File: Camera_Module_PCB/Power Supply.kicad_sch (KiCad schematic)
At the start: 27 parts, among them J1 SS-52400-002, SW1 SW_DIP_x01

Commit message: no
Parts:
- R5, R6, R7: value R_US -> 1K
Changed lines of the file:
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@@
 			)
 		)
-		(property "Value" "R_US"
+		(property "Value" "1K"
 			(at 139.7 71.1199 0)
 			(effects
@@
 			)
 		)
-		(property "Value" "R_US"
+		(property "Value" "1K"
 			(at 148.59 71.1199 0)
 			(effects
@@
 			)
 		)
-		(property "Value" "R_US"
+		(property "Value" "1K"
 			(at 157.48 71.1199 0)
 			(effects

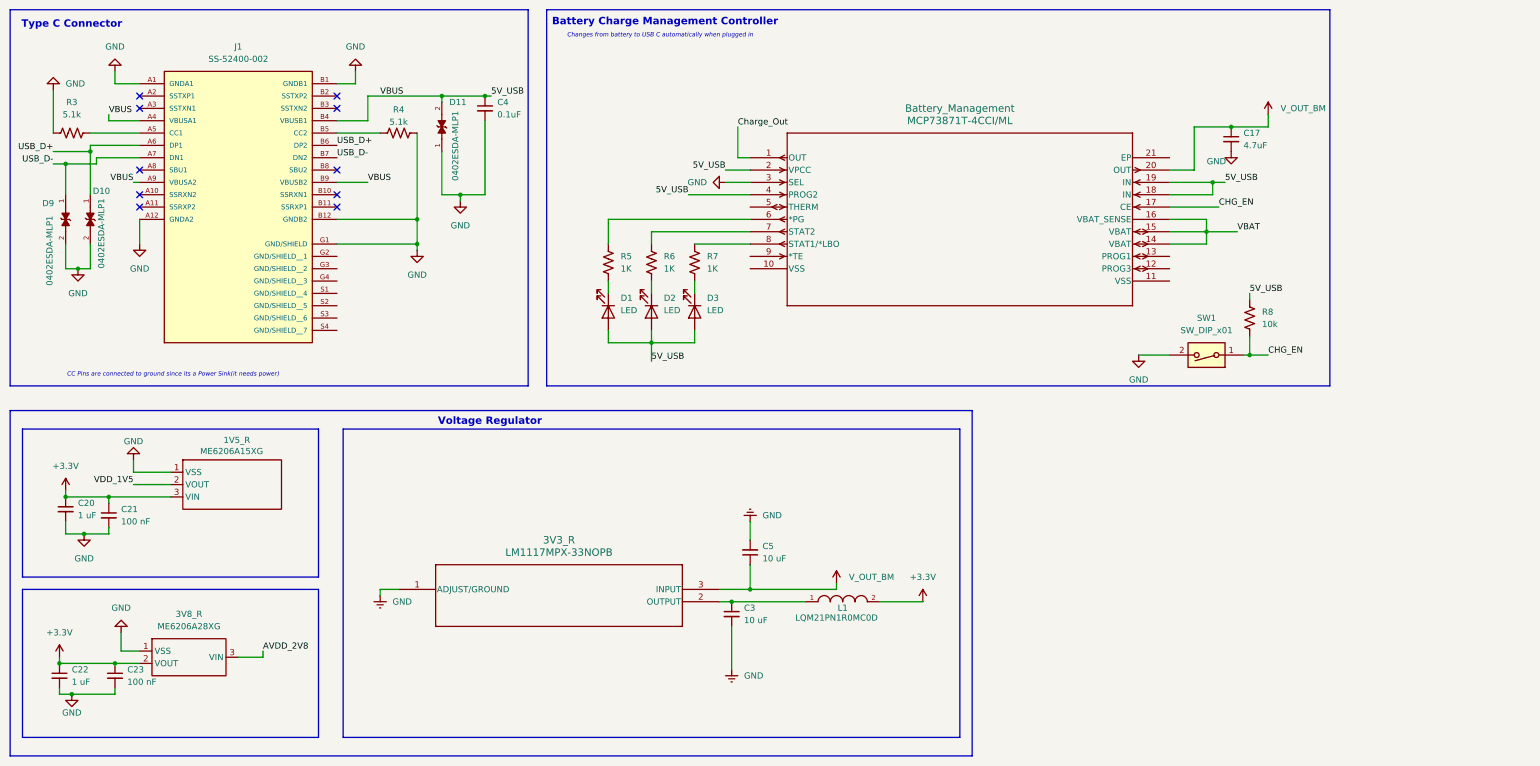
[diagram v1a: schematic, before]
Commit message: Compiled Footprints and Set up PCB layout
All of the footprints that correspond to the schematic symbols were properly referenced in the schematic annotations. The PCB layout was then updated to contain all of the appropriate footprints. Finally, a large ground filled zone was created with dimensions of about 42mm x 42mm as a starting base for the PCB size.
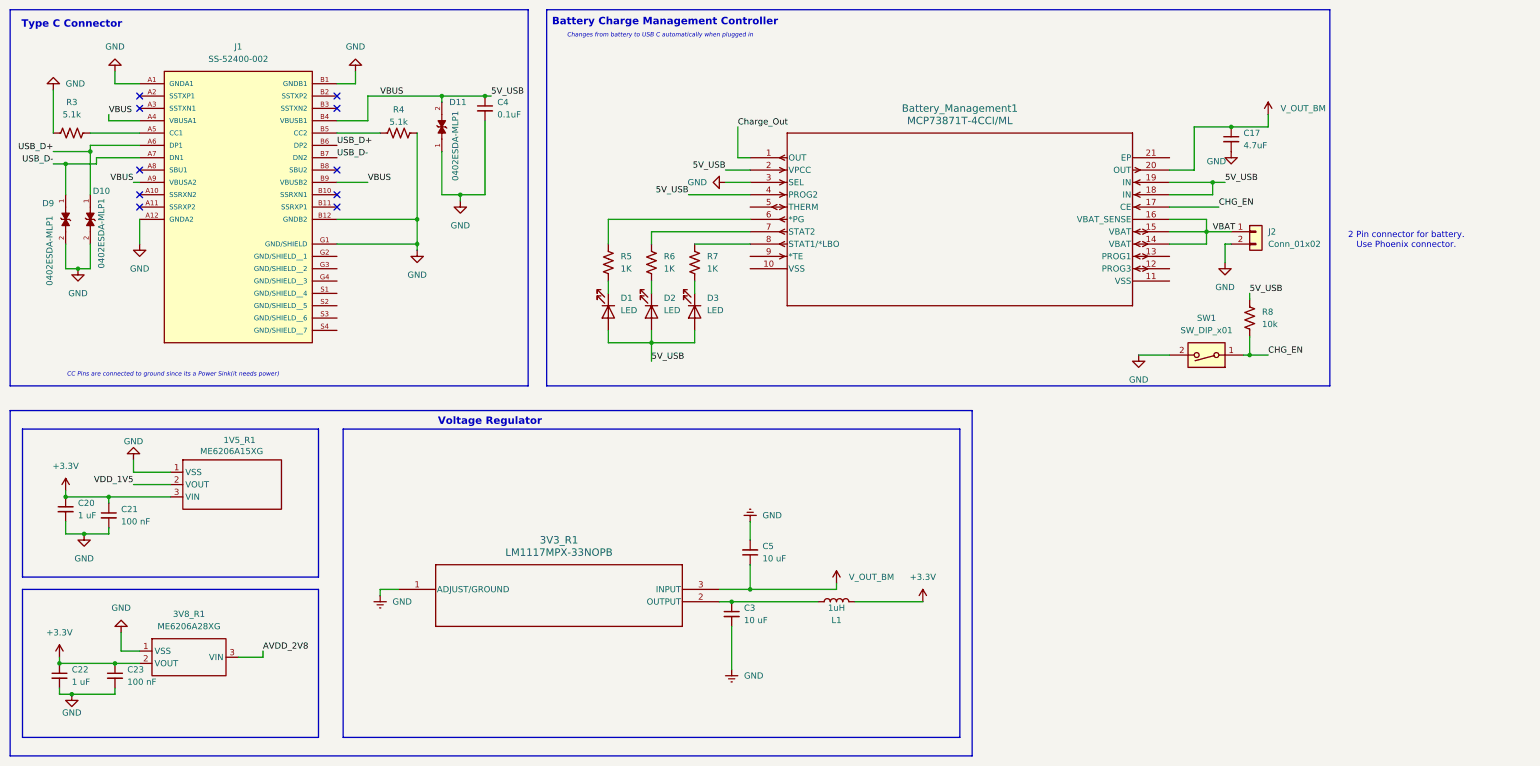
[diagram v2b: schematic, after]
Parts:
- removed L1: LQM21PN1R0MC0D, LQM21PN1R0MC0D:INDC2012X55N, symbol LMQ21PN1R0:LQM21PN1R0MC0D
- added J2: Conn_01x02, Connector_Phoenix_MSTB:PhoenixContact_MSTBA_2,5_2-G-5,08_1x02_P5.08mm_Horizontal, symbol Connector_Generic:Conn_01x02
- added L1: 1uH, Inductor_SMD:L_0603_1608Metric, symbol Device:L
- 3V3_R1: renamed from 3V3_R; footprint SOT223-318H_OSI -> LM1117MPX-33NOPB:SOT223-318H_OSI
- Battery_Management1: renamed from Battery_Management; footprint QFN20_4x4MC_MCH -> MCP73871T_4CCI_ML:QFN20_4x4MC_MCH
- C17, C20, C21, C22, C23, C3, C4, C5: footprint (none) -> Capacitor_SMD:C_0603_1608Metric
- D1, D2, D3: footprint (none) -> LED_SMD:LED_2010_5025Metric
- D10, D11, D9: footprint 0402ESDA-MLP1:ESD_0402ESDA-MLP1 -> ESP32CAM_Foorprints:ESD_0402ESDA-MLP1
- J1: footprint SS-52400-002:BELFUSE_SS-52400-002 -> ESP32CAM_Foorprints:BELFUSE_SS-52400-002
- R3, R4, R5, R6, R7, R8: footprint (none) -> Resistor_SMD:R_0603_1608Metric
- SW1: footprint (none) -> Button_Switch_THT:SW_DIP_SPSTx01_Slide_6.7x4.1mm_W7.62mm_P2.54mm_LowProfile
- renumbered 1V5_R to 1V5_R1, 3V8_R to 3V8_R1
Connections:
- net +3.3V: now also L1.2
- net GND: now also J2.2 (Pin_2)
- net VBAT: now also J2.1 (Pin_1)
- net at 3V3_R1.2 (OUTPUT), C3.1: now also L1.1
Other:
- note added: "2 Pin connector for battery. Use Phoenix connector."

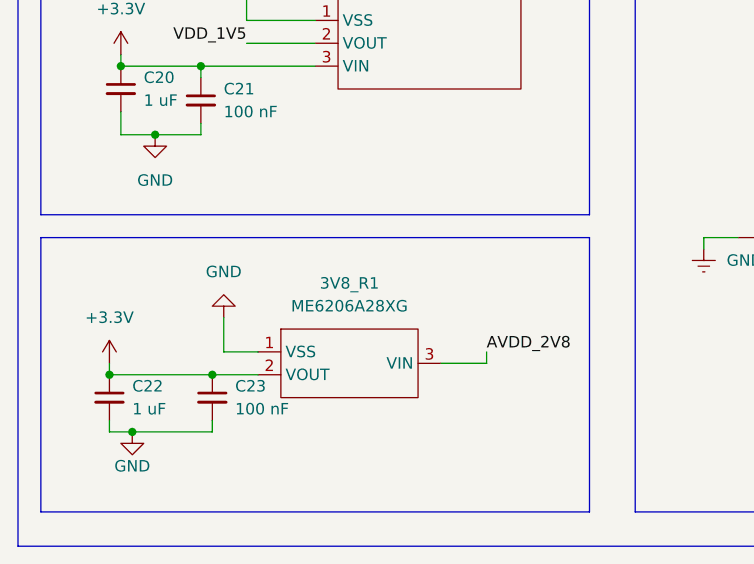
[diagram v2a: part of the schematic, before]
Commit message: Began early Layout for PCB
Moved most of the ICs into a general area layout for the PCB.
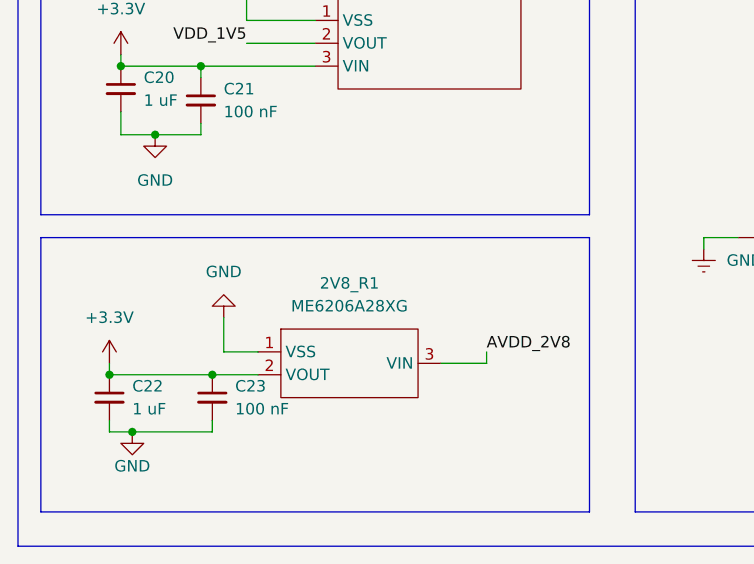
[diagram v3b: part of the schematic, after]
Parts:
- renumbered 3V8_R1 to 2V8_R1
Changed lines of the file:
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@@
 		(dnp no)
 		(fields_autoplaced yes)
-		(property "Reference" "3V8_R1"
+		(property "Reference" "2V8_R1"
 			(at 50.8 142.24 0)
 			(effects
@@
 			(project ""
 				(path "/e3d5a9d6-7dc8-43b3-bd64-189ae9cbab33/097e721d-c536-4567-9b5e-193861a3bee4"
-					(reference "3V8_R1")
+					(reference "2V8_R1")
 					(unit 1)
 				)

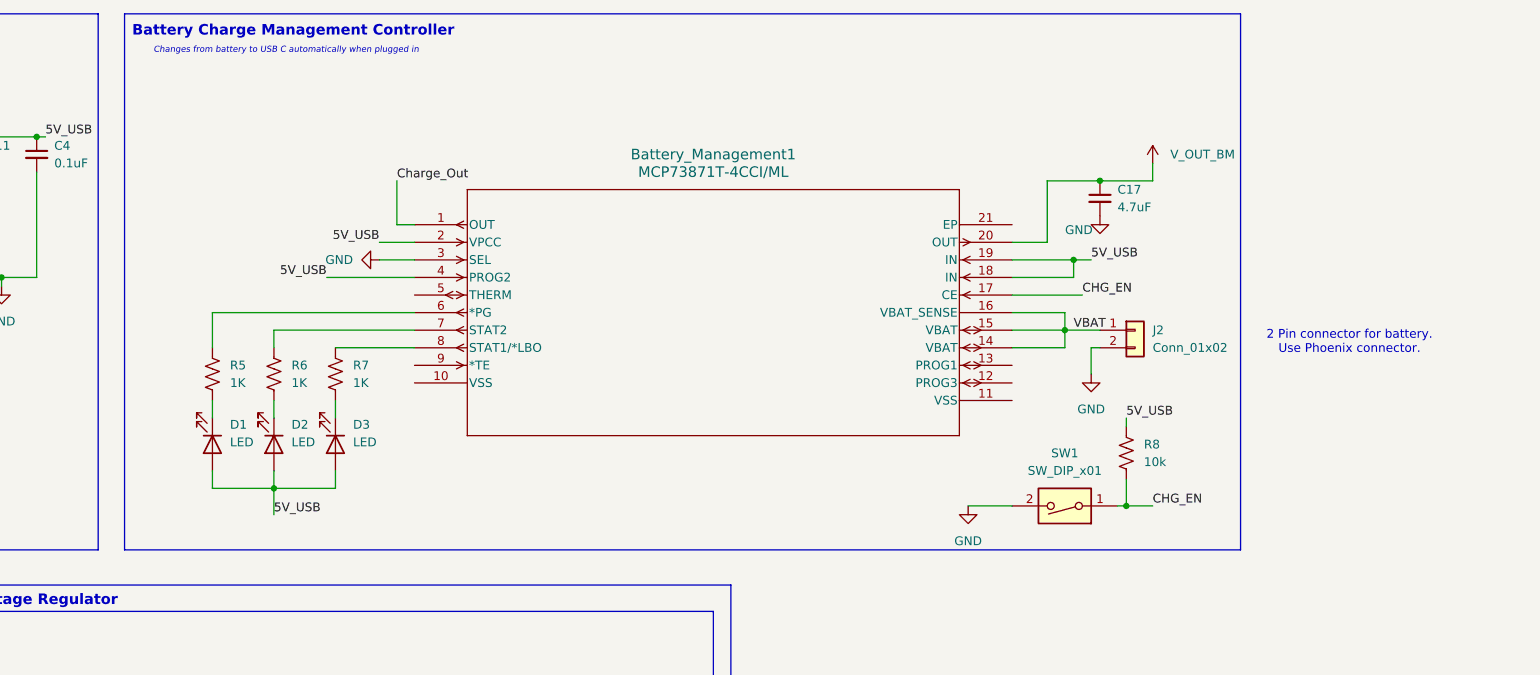
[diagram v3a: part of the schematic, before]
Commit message: Finished Schematic Except for a small few passives
Finished all of the connections in the schematic page and added a new LED driver. A small selection of passive elements must be given proper values after some calculations.
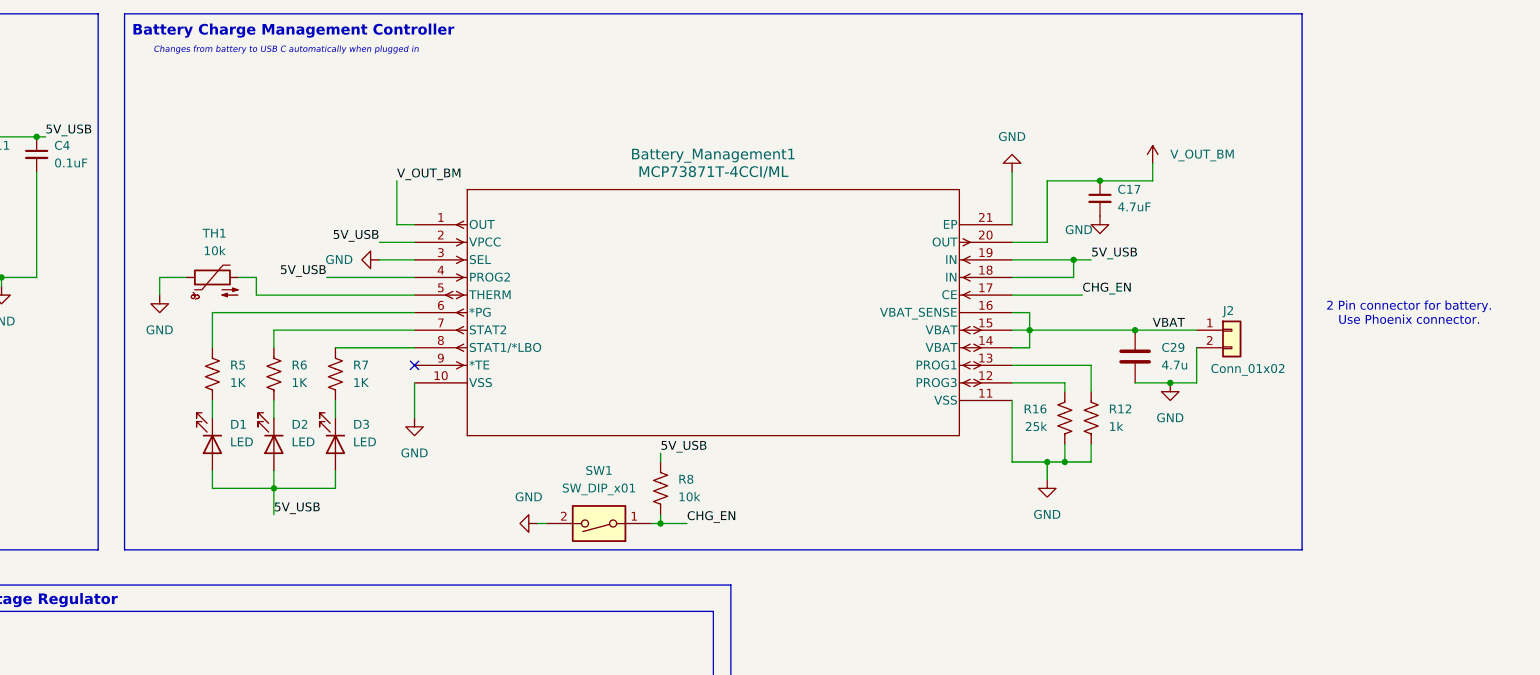
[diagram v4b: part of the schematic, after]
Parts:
- added C29: 4.7u, Capacitor_SMD:C_0603_1608Metric, symbol Device:C
- added R12: 1k, Resistor_SMD:R_0603_1608Metric, symbol Device:R_US
- added R16: 25k, Resistor_SMD:R_0603_1608Metric, symbol Device:R_US
- added TH1: 10k, Resistor_SMD:R_0603_1608Metric, symbol Device:Thermistor_NTC
- D1, D2, D3: footprint LED_SMD:LED_2010_5025Metric -> LED_SMD:LED_0603_1608Metric
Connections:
- net Charge_Out is gone; now on net V_OUT_BM: Battery_Management1.1 (OUT)
- net GND: now also Battery_Management1.10 (VSS), Battery_Management1.11 (VSS), Battery_Management1.21 (EP), C29.2, R12.2, R16.2, TH1.1
- net VBAT: now also C29.1
- net at Battery_Management1.12 (PROG3): now also R16.1
- net at Battery_Management1.13 (PROG1): now also R12.1
- net at Battery_Management1.5 (THERM): now also TH1.2
- no-connect marks 10 -> 11
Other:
- moved on the sheet: J2, R8, SW1

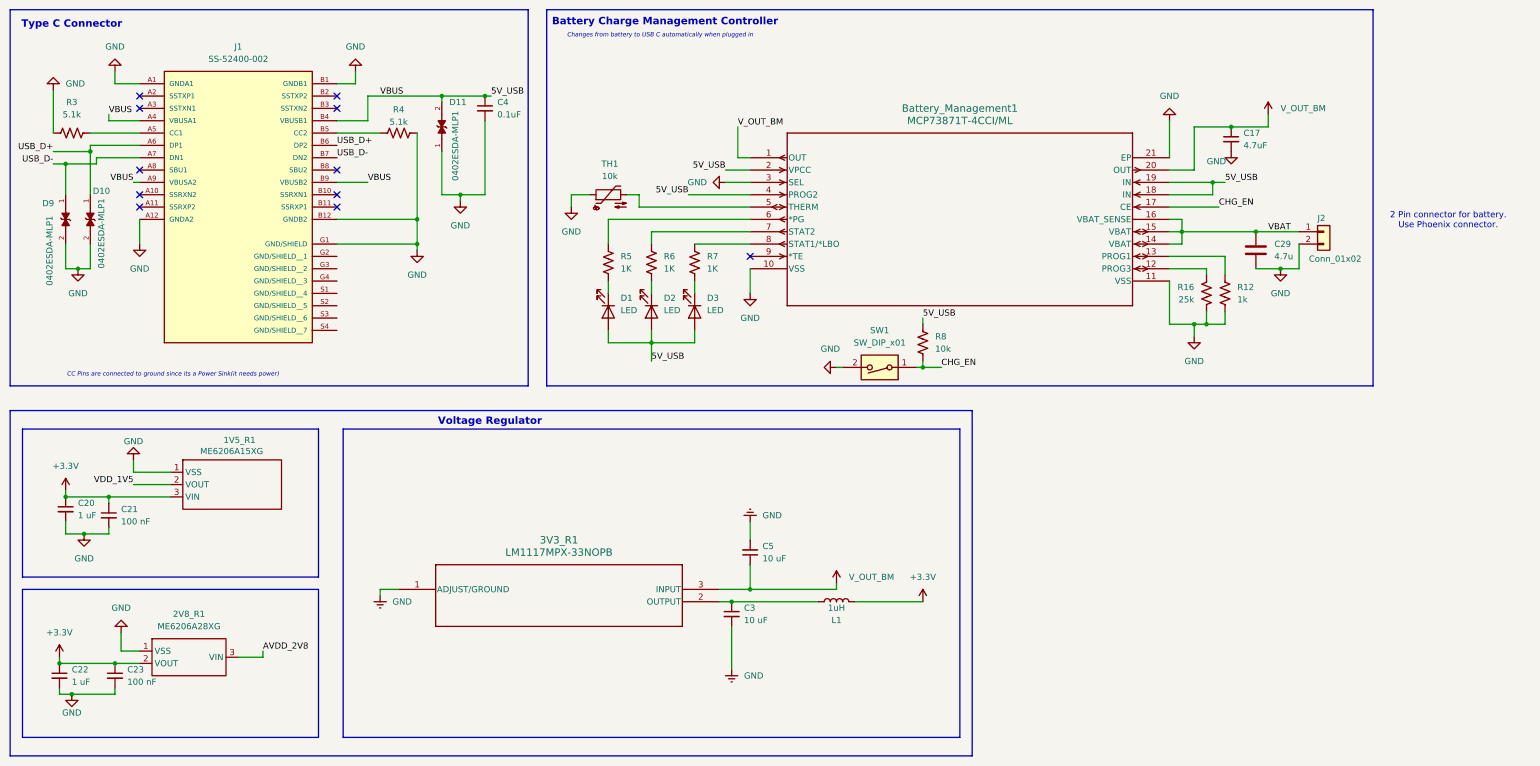
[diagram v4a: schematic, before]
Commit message: Made minor changes to schematic
Schematic is finished except for the inclusion of an RF antenna for Pin 1 of the ESP32. Waiting on team confirmation about its inclusion.
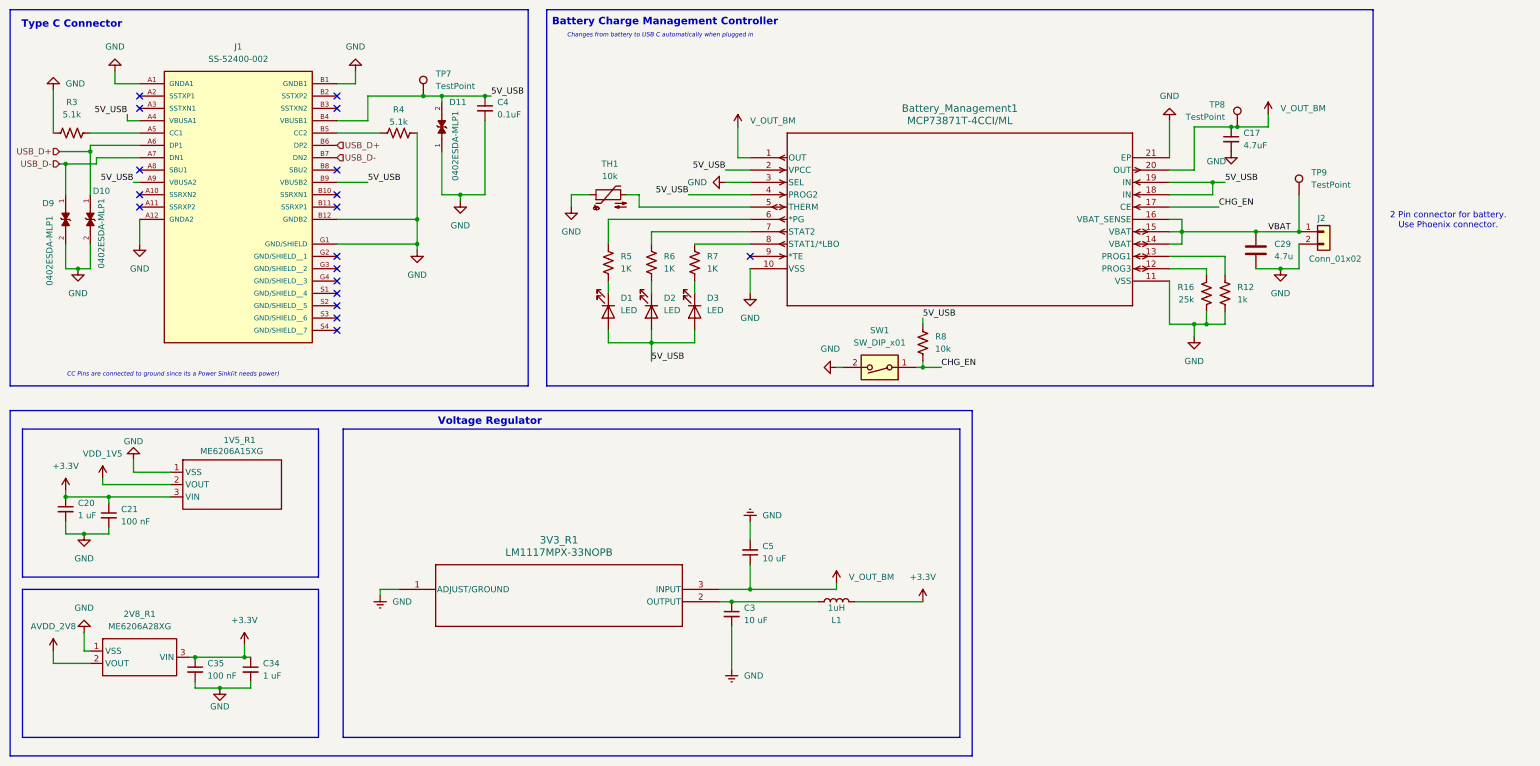
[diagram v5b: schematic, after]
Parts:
- removed C22: 1 uF, Capacitor_SMD:C_0603_1608Metric, symbol Device:C_Small
- removed C23: 100 nF, Capacitor_SMD:C_0603_1608Metric, symbol Device:C_Small
- added C34: 1 uF, Capacitor_SMD:C_0603_1608Metric, symbol Device:C_Small
- added C35: 100 nF, Capacitor_SMD:C_0603_1608Metric, symbol Device:C_Small
- added TP7, TP8, TP9: TestPoint, symbol Connector:TestPoint
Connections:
- net +3.3V: now also 2V8_R1.3 (VIN), C34.1, C35.1; no longer 2V8_R1.2 (VOUT)
- net 5V_USB: now also TP7.1
- net AVDD_2V8: now also 2V8_R1.2 (VOUT); no longer 2V8_R1.3 (VIN)
- net GND: now also C34.2, C35.2
- net VBAT: now also TP9.1
- net V_OUT_BM: now also TP8.1
- no-connect marks 11 -> 18
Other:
- moved on the sheet: 2V8_R1

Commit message: Made some schematic edits & continued work on layout
Made some minor adjustments for the schematic to prepare for review. The layout continues to be built.
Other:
- note added: "Ensure current is fine for LED pins"
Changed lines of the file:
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@@
+		)
+	)
+	(text "Ensure current is fine for\nLED pins\n"
+		(exclude_from_sim no)
+		(at 147.828 93.218 0)
+		(effects
+			(font
+				(size 1.27 1.27)
+			)
 		)
 	)

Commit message: Finished Power Supply
The power supply was finished for the ESP32 Chip and the board as a whole. A large plain was constructed in the third layer of the PCB to hold the 3.3V power supply from the regulator. Multiple traces have begun to be routed out of the ESP32 chip to be connected later on.
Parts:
- D10, D11, D9: DESCRIPTION ESD Suppressor Diode Polymer Bi-Dir 30V 2-Pin Case 0402(100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 -> (none)
- J2: footprint Connector_Phoenix_MSTB:PhoenixContact_MSTBA_2,5_2-G-5,08_1x02_P5.08mm_Horizontal -> ESP32CAM_Foorprints:PHOENIX_1725656

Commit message: Continued General Component Layout
More components were placed in general areas where they are predicted to remain. The two LDO voltage regulators for the camera power supply were connected to the main output voltage of the battery manager. The camera FFC connection along with other components were moved around the prepare for connections.
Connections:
- net +3.3V: no longer 1V5_R1.3 (VIN), 2V8_R1.3 (VIN), C20.1, C21.1, C34.1, C35.1
- net V_OUT_BM: now also 1V5_R1.3 (VIN), 2V8_R1.3 (VIN), C20.1, C21.1, C34.1, C35.1
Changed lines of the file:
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@@
 			)
 		)
-		(property "Value" "+3.3V"
+		(property "Value" "V_OUT_BM"
 			(at 25.4 111.76 0)
 			(show_name no)
@@
 			)
 		)
-		(property "Value" "+3.3V"
+		(property "Value" "V_OUT_BM"
 			(at 62.23 143.51 0)
 			(show_name no)
